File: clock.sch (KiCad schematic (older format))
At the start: 22 parts, among them SW1 SW_Push, SW2 SW_SPDT, U23 LM555xM, U24 74LS04, U25 74LS08, U26 74LS04, U27 74LS32, U28 LM555xM, U29 74LS04, U30 LM555xM

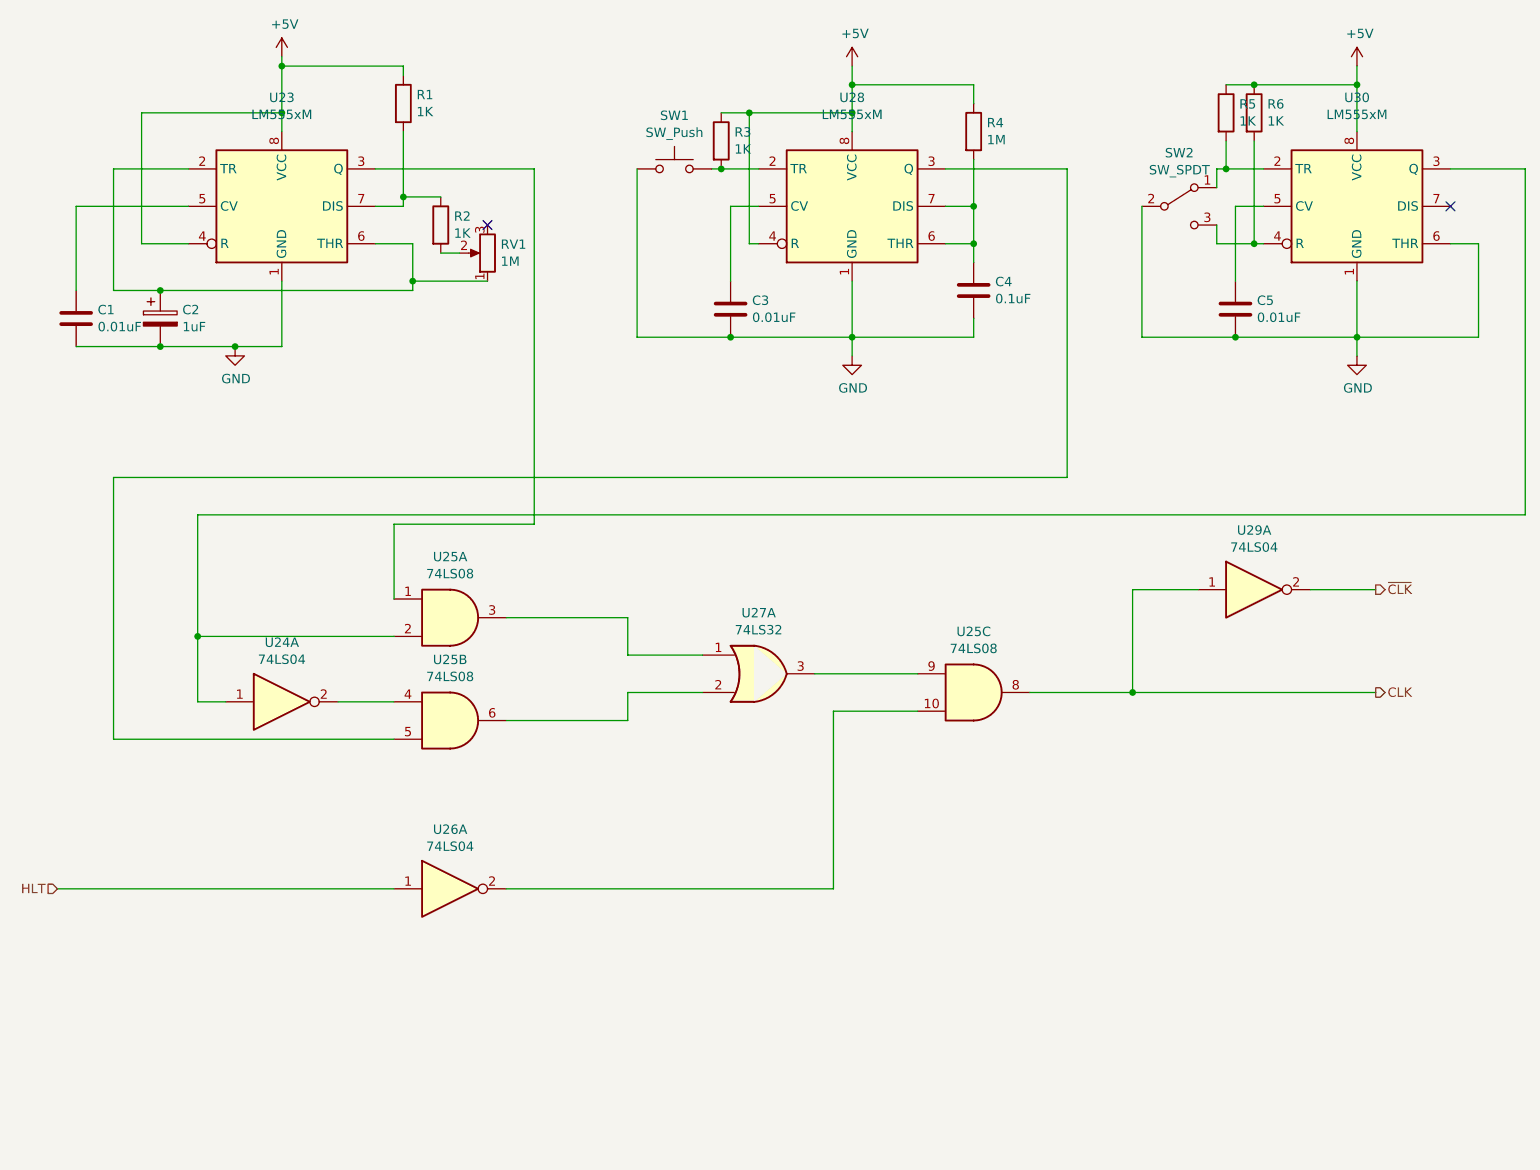
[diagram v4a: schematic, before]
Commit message: Fixed power for multi part comps
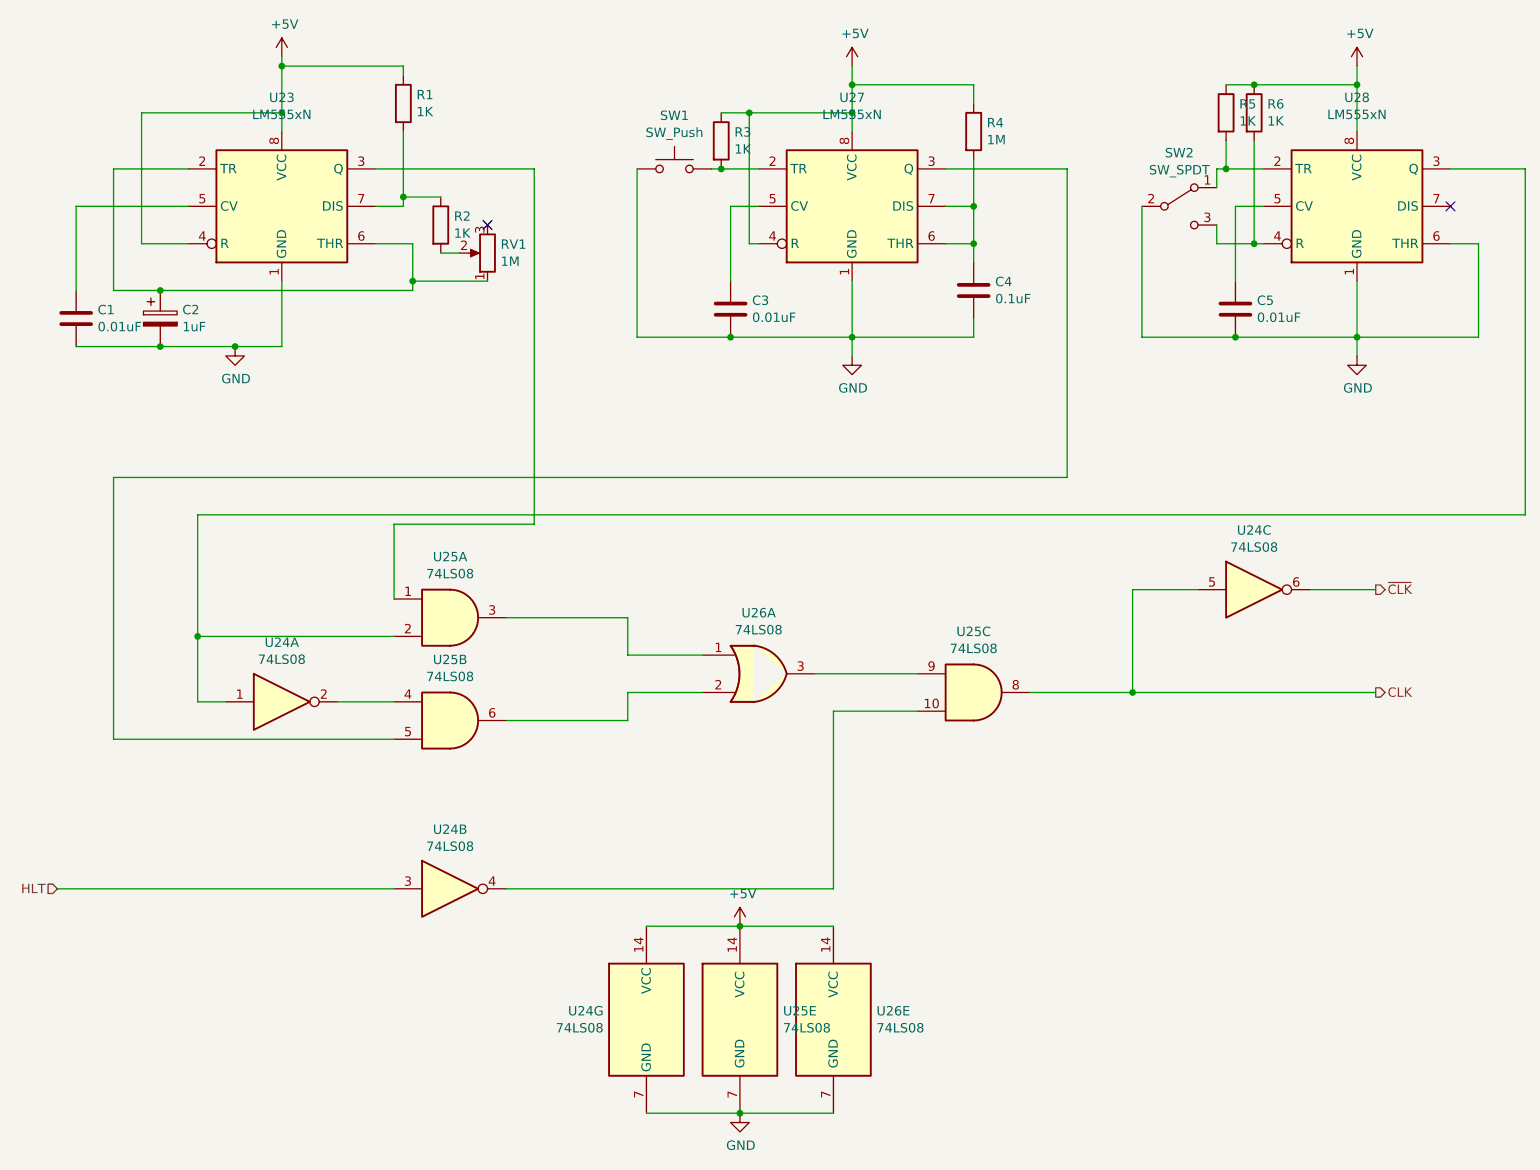
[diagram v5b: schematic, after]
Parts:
- removed U23, U28, U30: LM555xM, Package_SO:SOIC-8_3.9x4.9mm_P1.27mm, symbol Timer:LM555xM
- added U23, U27, U28: LM555xN, Package_DIP:DIP-8_W7.62mm, symbol Timer:LM555xN
- added unit 7 of U24
- added unit 5 of U25
- added unit 5 of U26
- U24: value 74LS04 -> 74LS08
- U24: renamed from U26; value 74LS04 -> 74LS08
- U24: renamed from U29; value 74LS04 -> 74LS08
- U26: renamed from U27; value 74LS32 -> 74LS08
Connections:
- net +5V: now also U23.4 (R), U23.8 (VCC), U24.14 (VCC), U25.14 (VCC), U26.14 (VCC), U27.4 (R), U27.8 (VCC), U28.8 (VCC)
- net CLK: now also U24.5; no longer U24.1
- net GND: now also U23.1 (GND), U24.7 (GND), U25.7 (GND), U26.7 (GND), U27.1 (GND), U28.1 (GND), U28.6 (THR)
- net HLT: now also U24.3; no longer U24.1
- net ~CLK: now also U24.6; no longer U24.2
- net at C2.1, RV1.1: now also U23.2 (TR), U23.6 (THR)
- net at U25.1: now also U23.3 (Q)
- net at C1.1: now also U23.5 (CV)
- net at R1.2, R2.1: now also U23.7 (DIS)
- net at R3.2, SW1.2: now also U27.2 (TR)
- net at U25.5: now also U27.3 (Q)
- net at C3.1: now also U27.5 (CV)
- net at C4.1, R4.2: now also U27.6 (THR), U27.7 (DIS)
- net at R5.2, SW2.1 (A): now also U28.2 (TR)
- net at U24.1, U25.2: now also U28.3 (Q)
- net at R6.2, SW2.3 (C): now also U28.4 (R)
- net at C5.1: now also U28.5 (CV)
- net at U25.10: now also U24.4; no longer U24.2
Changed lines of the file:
@@
 $EndDescr
 $Comp
-L Timer:LM555xM U23
-U 1 1 5F75E4EC
-P 2700 1900
-F 0 "U23" H 2700 2481 50  0000 C CNN
-F 1 "LM555xM" H 2700 2390 50  0000 C CNN
-F 2 "Package_SO:SOIC-8_3.9x4.9mm_P1.27mm" H 3550 1500 50  0001 C CNN
-F 3 "http://www.ti.com/lit/ds/symlink/lm555.pdf" H 3550 1500 50  0001 C CNN
-	1    2700 1900
-	1    0    0    -1
-$EndComp
-$Comp
-L Timer:LM555xM U28
-U 1 1 5F760F5B
-P 5750 1900
-F 0 "U28" H 5750 2481 50  0000 C CNN
-F 1 "LM555xM" H 5750 2390 50  0000 C CNN
-F 2 "Package_SO:SOIC-8_3.9x4.9mm_P1.27mm" H 6600 1500 50  0001 C CNN
-F 3 "http://www.ti.com/lit/ds/symlink/lm555.pdf" H 6600 1500 50  0001 C CNN
-	1    5750 1900
-	1    0    0    -1
-$EndComp
-$Comp
-L power:+5V #PWR072
+L power:+5V #PWR078
 U 1 1 5F76260D
 P 2700 1100
-F 0 "#PWR072" H 2700 950 50  0001 C CNN
+F 0 "#PWR078" H 2700 950 50  0001 C CNN
 F 1 "+5V" H 2715 1273 50  0000 C CNN
 F 2 "" H 2700 1100 50  0001 C CNN
@@
 $EndComp
 $Comp
-L power:GND #PWR074
+L power:GND #PWR082
 U 1 1 5F763381
 P 5750 2700
-F 0 "#PWR074" H 5750 2450 50  0001 C CNN
+F 0 "#PWR082" H 5750 2450 50  0001 C CNN
 F 1 "GND" H 5755 2527 50  0000 C CNN
 F 2 "" H 5750 2700 50  0001 C CNN
@@
 $EndComp
 $Comp
-L power:GND #PWR071
+L power:GND #PWR077
 U 1 1 5F7634B3
 P 2450 2650
-F 0 "#PWR071" H 2450 2400 50  0001 C CNN
+F 0 "#PWR077" H 2450 2400 50  0001 C CNN
 F 1 "GND" H 2455 2477 50  0000 C CNN
 F 2 "" H 2450 2650 50  0001 C CNN
@@
 $EndComp
 Wire Wire Line
-	1600 2350 1600 1900
-Wire Wire Line
 	1600 1900 2200 1900
 Wire Wire Line
@@
 Connection ~ 2450 2650
 $Comp
-L power:+5V #PWR073
+L power:+5V #PWR081
 U 1 1 5F76F8D8
 P 5750 1150
-F 0 "#PWR073" H 5750 1000 50  0001 C CNN
+F 0 "#PWR081" H 5750 1000 50  0001 C CNN
 F 1 "+5V" H 5765 1323 50  0000 C CNN
 F 2 "" H 5750 1150 50  0001 C CNN
@@
 Connection ~ 5050 1700
 $Comp
-L Timer:LM555xM U30
-U 1 1 5F785273
-P 8450 1900
-F 0 "U30" H 8450 2481 50  0000 C CNN
-F 1 "LM555xM" H 8450 2390 50  0000 C CNN
-F 2 "Package_SO:SOIC-8_3.9x4.9mm_P1.27mm" H 9300 1500 50  0001 C CNN
-F 3 "http://www.ti.com/lit/ds/symlink/lm555.pdf" H 9300 1500 50  0001 C CNN
-	1    8450 1900
-	1    0    0    -1
-$EndComp
-$Comp
-L power:GND #PWR076
+L power:GND #PWR084
 U 1 1 5F785279
 P 8450 2700
-F 0 "#PWR076" H 8450 2450 50  0001 C CNN
+F 0 "#PWR084" H 8450 2450 50  0001 C CNN
 F 1 "GND" H 8455 2527 50  0000 C CNN
 F 2 "" H 8450 2700 50  0001 C CNN
@@
 $EndComp
 $Comp
-L power:+5V #PWR075
+L power:+5V #PWR083
 U 1 1 5F78527F
 P 8450 1150
-F 0 "#PWR075" H 8450 1000 50  0001 C CNN
+F 0 "#PWR083" H 8450 1000 50  0001 C CNN
 F 1 "+5V" H 8465 1323 50  0000 C CNN
 F 2 "" H 8450 1150 50  0001 C CNN
@@
 $EndComp
 $Comp
-L 74xx:74LS32 U27
+L 74xx:74LS32 U26
 U 1 1 5F7C6F12
 P 5250 4400
-F 0 "U27" H 5250 4725 50  0000 C CNN
-F 1 "74LS32" H 5250 4634 50  0000 C CNN
+F 0 "U26" H 5250 4725 50  0000 C CNN
+F 1 "74LS08" H 5250 4634 50  0000 C CNN
 F 2 "Package_DIP:DIP-14_W7.62mm" H 5250 4400 50  0001 C CNN
-F 3 "http://www.ti.com/lit/gpn/sn74LS32" H 5250 4400 50  0001 C CNN
+F 3 "http://www.ti.com/lit/gpn/sn74LS08" H 5250 4400 50  0001 C CNN
 	1    5250 4400
 	1    0    0    -1
@@
 P 2700 4550
 F 0 "U24" H 2700 4867 50  0000 C CNN
-F 1 "74LS04" H 2700 4776 50  0000 C CNN
+F 1 "74LS08" H 2700 4776 50  0000 C CNN
 F 2 "Package_DIP:DIP-14_W7.62mm" H 2700 4550 50  0001 C CNN
-F 3 "http://www.ti.com/lit/gpn/sn74LS04" H 2700 4550 50  0001 C CNN
+F 3 "http://www.ti.com/lit/gpn/sn74LS08" H 2700 4550 50  0001 C CNN
 	1    2700 4550
 	1    0    0    -1
 $EndComp
 $Comp
-L 74xx:74LS04 U26
-U 1 1 5F7D01D9
+L 74xx:74LS04 U24
+U 2 1 5F7D01D9
 P 3600 5550
-F 0 "U26" H 3600 5867 50  0000 C CNN
-F 1 "74LS04" H 3600 5776 50  0000 C CNN
+F 0 "U24" H 3600 5867 50  0000 C CNN
+F 1 "74LS08" H 3600 5776 50  0000 C CNN
 F 2 "Package_DIP:DIP-14_W7.62mm" H 3600 5550 50  0001 C CNN
-F 3 "http://www.ti.com/lit/gpn/sn74LS04" H 3600 5550 50  0001 C CNN
-	1    3600 5550
-	1    0    0    -1
-$EndComp
-$Comp
-L 74xx:74LS04 U29
-U 1 1 5F7D1AFC
+F 3 "http://www.ti.com/lit/gpn/sn74LS08" H 3600 5550 50  0001 C CNN
+	2    3600 5550
+	1    0    0    -1
+$EndComp
+$Comp
+L 74xx:74LS04 U24
+U 3 1 5F7D1AFC
 P 7900 3950
-F 0 "U29" H 7900 4267 50  0000 C CNN
-F 1 "74LS04" H 7900 4176 50  0000 C CNN
+F 0 "U24" H 7900 4267 50  0000 C CNN
+F 1 "74LS08" H 7900 4176 50  0000 C CNN
 F 2 "Package_DIP:DIP-14_W7.62mm" H 7900 3950 50  0001 C CNN
-F 3 "http://www.ti.com/lit/gpn/sn74LS04" H 7900 3950 50  0001 C CNN
-	1    7900 3950
+F 3 "http://www.ti.com/lit/gpn/sn74LS08" H 7900 3950 50  0001 C CNN
+	3    7900 3950
 	1    0    0    -1
 $EndComp
@@
 Text HLabel 8550 4500 2    50   Output ~ 0
 CLK
+Wire Wire Line
+	4650 5750 5150 5750
+Wire Wire Line
+	5650 5750 5150 5750
+Connection ~ 5150 5750
+Wire Wire Line
+	4650 6750 5150 6750
+Wire Wire Line
+	5650 6750 5150 6750
+Connection ~ 5150 6750
+$Comp
+L power:+5V #PWR079
+U 1 1 6081D7D4
+P 5150 5750
+F 0 "#PWR079" H 5150 5600 50  0001 C CNN
+F 1 "+5V" H 5165 5923 50  0000 C CNN
+F 2 "" H 5150 5750 50  0001 C CNN
+F 3 "" H 5150 5750 50  0001 C CNN
+	1    5150 5750
+	1    0    0    -1
+$EndComp
+$Comp
+L power:GND #PWR080
+U 1 1 6081E349
+P 5150 6750
+F 0 "#PWR080" H 5150 6500 50  0001 C CNN
+F 1 "GND" H 5155 6577 50  0000 C CNN
+F 2 "" H 5150 6750 50  0001 C CNN
+F 3 "" H 5150 6750 50  0001 C CNN
+	1    5150 6750
+	1    0    0    -1
+$EndComp
+$Comp
+L 74xx:74LS04 U24
+U 7 1 6085491F
+P 4650 6250
+F 0 "U24" H 4421 6296 50  0000 R CNN
+F 1 "74LS08" H 4421 6205 50  0000 R CNN
+F 2 "Package_DIP:DIP-14_W7.62mm" H 4650 6250 50  0001 C CNN
+F 3 "http://www.ti.com/lit/gpn/sn74LS08" H 4650 6250 50  0001 C CNN
+	7    4650 6250
+	1    0    0    -1
+$EndComp
+$Comp
+L 74xx:74LS08 U25
+U 5 1 6085870D
+P 5150 6250
+F 0 "U25" H 5380 6296 50  0000 L CNN
+F 1 "74LS08" H 5380 6205 50  0000 L CNN
+F 2 "Package_DIP:DIP-14_W7.62mm" H 5150 6250 50  0001 C CNN
+F 3 "http://www.ti.com/lit/gpn/sn74LS08" H 5150 6250 50  0001 C CNN
+	5    5150 6250
+	1    0    0    -1
+$EndComp
+$Comp
+L 74xx:74LS32 U26
+U 5 1 608654F6
+P 5650 6250
+F 0 "U26" H 5880 6296 50  0000 L CNN
+F 1 "74LS08" H 5880 6205 50  0000 L CNN
+F 2 "Package_DIP:DIP-14_W7.62mm" H 5650 6250 50  0001 C CNN
+F 3 "http://www.ti.com/lit/gpn/sn74LS08" H 5650 6250 50  0001 C CNN
+	5    5650 6250
+	1    0    0    -1
+$EndComp
+$Comp
+L Timer:LM555xN U23
+U 1 1 60AA52FF
+P 2700 1900
+F 0 "U23" H 2700 2481 50  0000 C CNN
+F 1 "LM555xN" H 2700 2390 50  0000 C CNN
+F 2 "Package_DIP:DIP-8_W7.62mm" H 3350 1500 50  0001 C CNN
+F 3 "http://www.ti.com/lit/ds/symlink/lm555.pdf" H 3550 1500 50  0001 C CNN
+	1    2700 1900
+	1    0    0    -1
+$EndComp
+Wire Wire Line
+	1600 1900 1600 2350
+$Comp
+L Timer:LM555xN U27
+U 1 1 60AB8137
+P 5750 1900
+F 0 "U27" H 5750 2481 50  0000 C CNN
+F 1 "LM555xN" H 5750 2390 50  0000 C CNN
+F 2 "Package_DIP:DIP-8_W7.62mm" H 6400 1500 50  0001 C CNN
+F 3 "http://www.ti.com/lit/ds/symlink/lm555.pdf" H 6600 1500 50  0001 C CNN
+	1    5750 1900
+	1    0    0    -1
+$EndComp
+$Comp
+L Timer:LM555xN U28
+U 1 1 60AB9E78
+P 8450 1900
+F 0 "U28" H 8450 2481 50  0000 C CNN
+F 1 "LM555xN" H 8450 2390 50  0000 C CNN
+F 2 "Package_DIP:DIP-8_W7.62mm" H 9100 1500 50  0001 C CNN
+F 3 "http://www.ti.com/lit/ds/symlink/lm555.pdf" H 9300 1500 50  0001 C CNN
+	1    8450 1900
+	1    0    0    -1
+$EndComp
 $EndSCHEMATC

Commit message: Various Fixes
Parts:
- U24: value 74LS08 -> 74LS04
- U26: value 74LS08 -> 74LS32
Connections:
- no-connect marks 2 -> 3
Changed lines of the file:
@@
 P 5250 4400
 F 0 "U26" H 5250 4725 50  0000 C CNN
-F 1 "74LS08" H 5250 4634 50  0000 C CNN
+F 1 "74LS32" H 5250 4634 50  0000 C CNN
 F 2 "Package_DIP:DIP-14_W7.62mm" H 5250 4400 50  0001 C CNN
 F 3 "http://www.ti.com/lit/gpn/sn74LS08" H 5250 4400 50  0001 C CNN
@@
 P 2700 4550
 F 0 "U24" H 2700 4867 50  0000 C CNN
-F 1 "74LS08" H 2700 4776 50  0000 C CNN
+F 1 "74LS04" H 2700 4776 50  0000 C CNN
 F 2 "Package_DIP:DIP-14_W7.62mm" H 2700 4550 50  0001 C CNN
 F 3 "http://www.ti.com/lit/gpn/sn74LS08" H 2700 4550 50  0001 C CNN
@@
 P 3600 5550
 F 0 "U24" H 3600 5867 50  0000 C CNN
-F 1 "74LS08" H 3600 5776 50  0000 C CNN
+F 1 "74LS04" H 3600 5776 50  0000 C CNN
 F 2 "Package_DIP:DIP-14_W7.62mm" H 3600 5550 50  0001 C CNN
 F 3 "http://www.ti.com/lit/gpn/sn74LS08" H 3600 5550 50  0001 C CNN
@@
 P 7900 3950
 F 0 "U24" H 7900 4267 50  0000 C CNN
-F 1 "74LS08" H 7900 4176 50  0000 C CNN
+F 1 "74LS04" H 7900 4176 50  0000 C CNN
 F 2 "Package_DIP:DIP-14_W7.62mm" H 7900 3950 50  0001 C CNN
 F 3 "http://www.ti.com/lit/gpn/sn74LS08" H 7900 3950 50  0001 C CNN
@@
 P 4650 6250
 F 0 "U24" H 4421 6296 50  0000 R CNN
-F 1 "74LS08" H 4421 6205 50  0000 R CNN
+F 1 "74LS04" H 4421 6205 50  0000 R CNN
 F 2 "Package_DIP:DIP-14_W7.62mm" H 4650 6250 50  0001 C CNN
 F 3 "http://www.ti.com/lit/gpn/sn74LS08" H 4650 6250 50  0001 C CNN
@@
 P 5650 6250
 F 0 "U26" H 5880 6296 50  0000 L CNN
-F 1 "74LS08" H 5880 6205 50  0000 L CNN
+F 1 "74LS32" H 5880 6205 50  0000 L CNN
 F 2 "Package_DIP:DIP-14_W7.62mm" H 5650 6250 50  0001 C CNN
 F 3 "http://www.ti.com/lit/gpn/sn74LS08" H 5650 6250 50  0001 C CNN
@@
 	1    0    0    -1
 $EndComp
+NoConn ~ 5450 5050
 $EndSCHEMATC
